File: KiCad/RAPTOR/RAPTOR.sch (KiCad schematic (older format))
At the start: 49 parts, among them J1 SOLC_CONN, J10 EXT_LED3, J11 SRVOL_CONN, J12 SRVOR_CONN, J13 HOTWIRE_CONN, J14 RBF_CONN, J15 EEPROM_BTN_CONN, J16 SOLC_SW_CONN, J17 SOLP_SW_CONN, J18 CONN_BUZZER, J2 SOLP_CONN, J3 JST_2MM_MALE, J4 CONN_LED_FIX, J5 CONN_SOLP_LED, J6 CONN_SOLC_LED, J7 EXT_LED0, J8 EXT_LED1, J9 EXT_LED2, P1 Power, P2 Analog, P3 Digital, P4 Digital, P5 CONN_01X01, P6 CONN_01X01, P7 CONN_01X01, P8 CONN_01X01, Q1 MOSFET-NCH-STQ2NK60ZR-AP, Q2 MOSFET-NCH-STQ2NK60ZR-AP, Q3 MOSFET-NCH-STQ2NK60ZR-AP, Q4 MOSFET-NCH-STQ2NK60ZR-AP, Q5 MOSFET-NCH-STQ2NK60ZR-AP, U1 BMP280 Breakout, U2 BNO055 Breakout, U3 OpenLog, U4 AdafruitGPS, U5 U3V12F12, U6 D24V550F5

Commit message: Added Teensy
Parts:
- removed J16: SOLC_SW_CONN, RAPTOR_footprints:Molex-2pin, symbol RAPTOR-rescue:CONN_02-SparkFun-Connectors
- removed J17: SOLP_SW_CONN, RAPTOR_footprints:Molex-2pin, symbol RAPTOR-rescue:CONN_02-SparkFun-Connectors
- removed J5: CONN_SOLP_LED, RAPTOR_footprints:Molex-2pin, symbol RAPTOR-rescue:CONN_02-SparkFun-Connectors
- removed J6: CONN_SOLC_LED, RAPTOR_footprints:Molex-2pin, symbol RAPTOR-rescue:CONN_02-SparkFun-Connectors
- removed P1: Power, RAPTOR_footprints:Socket_Strip_Arduino_1x08, symbol Connector_Generic:Conn_01x08
- removed P2: Analog, RAPTOR_footprints:Arduino_Analog_06, symbol RAPTOR-rescue:Arduino_Analog_Conn
- removed P3: Digital, RAPTOR_footprints:Arduino_x10_Digital, symbol RAPTOR-rescue:Arduino_Digital_01x10_Conn
- removed P4: Digital, RAPTOR_footprints:Arduino_x08_Digital, symbol RAPTOR-rescue:Arduino_Digital_8
- removed P5, P6, P7, P8: CONN_01X01, Socket_Arduino_Uno:Arduino_1pin, symbol Connector_Generic:Conn_01x01
- removed R3, R4: 100OHM-0603-1_10W-1%, RAPTOR_footprints:Resistor, symbol RAPTOR-rescue:100OHM-0603-1_10W-1%-SparkFun-Resistors
- removed R6, R7: 4.7KOHM-0603-1_10W-1%, RAPTOR_footprints:Resistor, symbol RAPTOR-rescue:4.7KOHM-0603-1_10W-1%-SparkFun-Resistors
- added U?: Teensy3.2, symbol teensy:Teensy3.2
- J15: value EEPROM_BTN_CONN -> EEP_BTN_CONN
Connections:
- net labels added: EEP_BTN
- net labels removed: A4(SDA), A5(SCL), AREF, EEPROM_BTN, IOREF, LEDC_DTA, LEDP_DTA, Reset, SOLC_SW, SOLP_SW
- wire segments 182 -> 139
- no-connect marks 18 -> 13
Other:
- note removed: "1"
- note removed: "Holes"
- note removed: "Shield for Arduino that uses\nthe same pin disposition\nlike "Uno" board Rev 3."
- moved on the sheet: J13, J14, J15, J3, Q5, R5, R8

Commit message: Removed 12v Step Up from schematic.
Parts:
- removed U5: U3V12F12, RAPTOR_footprints:U3V12F12, symbol RAPTOR-rescue:U3V12F12
- U?: symbol teensy:Teensy3.2 -> RAPTOR-rescue:Teensy3.2-teensy
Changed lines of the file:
@@
 EESchema Schematic File Version 4
 LIBS:RAPTOR-cache
-EELAYER 26 0
+EELAYER 30 0
 EELAYER END
 $Descr USLetter 11000 8500
@@
 $EndComp
 $Comp
-L power:GND #PWR012
-U 1 1 5C40FAEF
-P 3550 2400
-F 0 "#PWR012" H 3550 2150 50  0001 C CNN
-F 1 "GND" H 3555 2227 50  0000 C CNN
-F 2 "" H 3550 2400 50  0001 C CNN
-F 3 "" H 3550 2400 50  0001 C CNN
-	1    3550 2400
-	1    0    0    -1
-$EndComp
-Wire Wire Line
-	3550 2250 3550 2400
-$Comp
-L power:+7.5V #PWR011
-U 1 1 5C42772B
-P 3000 1900
-F 0 "#PWR011" H 3000 1750 50  0001 C CNN
-F 1 "+7.5V" H 3015 2073 50  0001 C CNN
-F 2 "" H 3000 1900 50  0001 C CNN
-F 3 "" H 3000 1900 50  0001 C CNN
-F 4 "+7.4V" H 3015 2073 50  0000 C CNN "Real Value"
-	1    3000 1900
-	1    0    0    -1
-$EndComp
-Wire Wire Line
-	3250 1950 3000 1950
-Wire Wire Line
-	3850 1950 4100 1950
-$Comp
-L power:+12V #PWR013
-U 1 1 5C4334FC
-P 4100 1900
-F 0 "#PWR013" H 4100 1750 50  0001 C CNN
-F 1 "+12V" H 4115 2165 50  0000 C CNN
-F 2 "" H 4100 1900 50  0001 C CNN
-F 3 "" H 4100 1900 50  0001 C CNN
-F 4 "(TO SOLENOID)" H 4115 2074 50  0000 C CNN "Note"
-	1    4100 1900
-	1    0    0    -1
-$EndComp
-$Comp
 L power:+5V #PWR014
 U 1 1 5C442A87
@@
 	1    0    0    -1
 $EndComp
-Wire Wire Line
-	3000 1950 3000 1900
-Wire Wire Line
-	4100 1950 4100 1900
 $Comp
 L power:GND #PWR016
@@
 F 3 "" H 4950 3100 50  0001 C CNN
 	1    4950 3100
-	1    0    0    -1
-$EndComp
-$Comp
-L RAPTOR-rescue:U3V12F12 U5
-U 1 1 5C3DF905
-P 3550 1950
-F 0 "U5" H 3550 2192 50  0000 C CNN
-F 1 "U3V12F12" H 3550 2101 50  0000 C CNN
-F 2 "RAPTOR_footprints:U3V12F12" H 3550 2200 50  0001 C CNN
-F 3 "" H 3550 2200 50  0001 C CNN
-	1    3550 1950
 	1    0    0    -1
 $EndComp
@@
 	2800 3500 2650 3500
 $Comp
-L teensy:Teensy3.2 U?
+L RAPTOR-rescue:Teensy3.2-teensy U?
 U 1 1 5D836A4E
 P 9200 2150

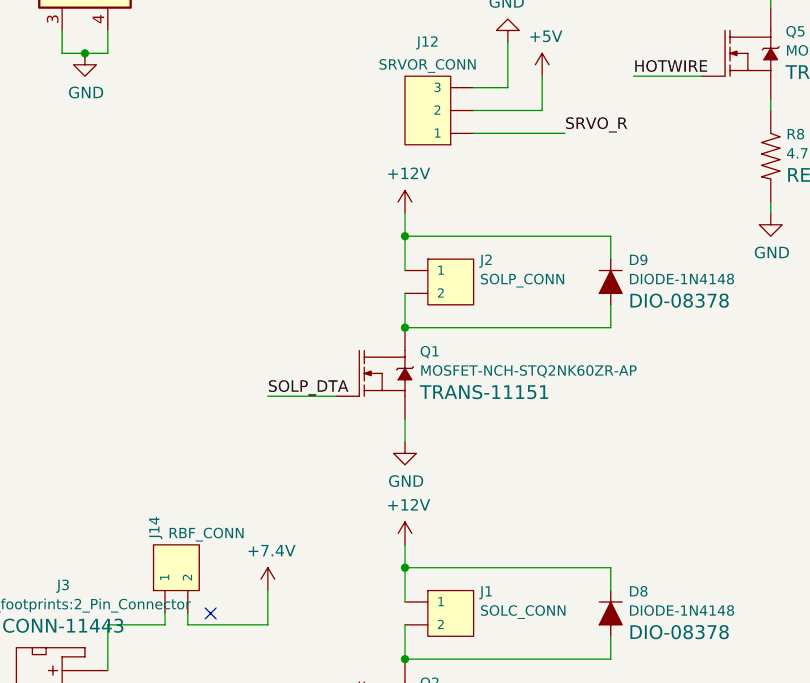
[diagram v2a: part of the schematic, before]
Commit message: Swapped +12V references with +7.4V references.
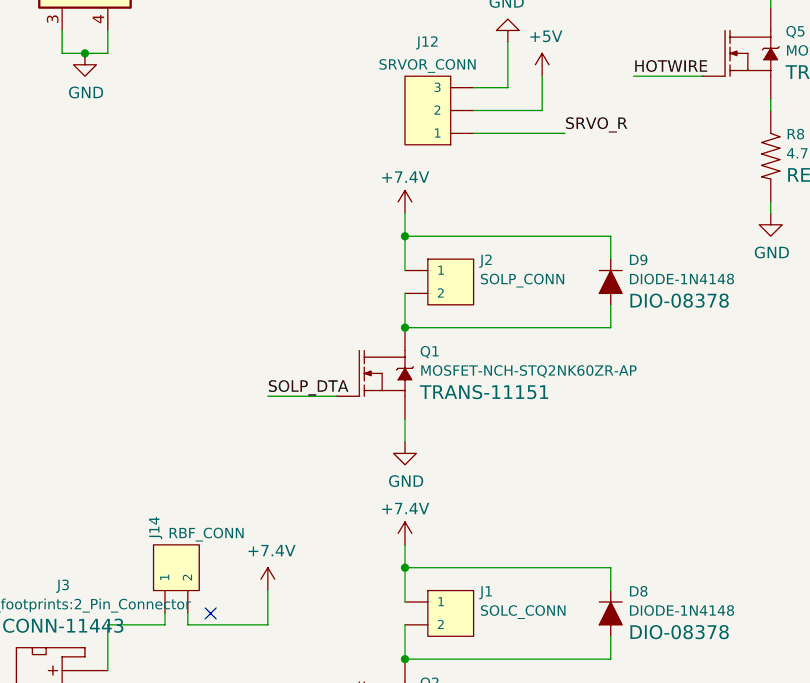
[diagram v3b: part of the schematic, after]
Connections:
- net +12V is gone; now on net +7.5V: D8.C, D9.C, J1.1, J2.1
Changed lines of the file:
@@
 	5550 1000 5550 850
-$Comp
-L power:+12V #PWR0113
-U 1 1 5BE8A086
-P 4950 2100
-F 0 "#PWR0113" H 4950 1950 50  0001 C CNN
-F 1 "+12V" H 4965 2273 50  0000 C CNN
-F 2 "" H 4950 2100 50  0001 C CNN
-F 3 "" H 4950 2100 50  0001 C CNN
-	1    4950 2100
-	1    0    0    -1
-$EndComp
 $Comp
 L RAPTOR-rescue:MOSFET-NCH-2N7002PW-SparkFun-DiscreteSemi Q1
@@
 	5850 2600 4950 2600
 $Comp
-L power:+12V #PWR05
+L power:+7.5V #PWR05
 U 1 1 5C55623C
 P 4950 3550
 F 0 "#PWR05" H 4950 3400 50  0001 C CNN
-F 1 "+12V" H 4965 3723 50  0000 C CNN
+F 1 "+7.5V" H 4965 3723 50  0001 C CNN
 F 2 "" H 4950 3550 50  0001 C CNN
 F 3 "" H 4950 3550 50  0001 C CNN
+F 4 "+7.4V" H 4950 3707 50  0000 C CNN "Real Value"
 	1    4950 3550
 	1    0    0    -1
@@
 Wire Wire Line
 	7950 800  7950 700
+$Comp
+L power:+7.5V #PWR0113
+U 1 1 5BE8A086
+P 4950 2100
+F 0 "#PWR0113" H 4950 1950 50  0001 C CNN
+F 1 "+7.5V" H 4965 2273 50  0001 C CNN
+F 2 "" H 4950 2100 50  0001 C CNN
+F 3 "" H 4950 2100 50  0001 C CNN
+F 4 "+7.4V" H 4950 2257 50  0000 C CNN "Real Value"
+	1    4950 2100
+	1    0    0    -1
+$EndComp
 $EndSCHEMATC

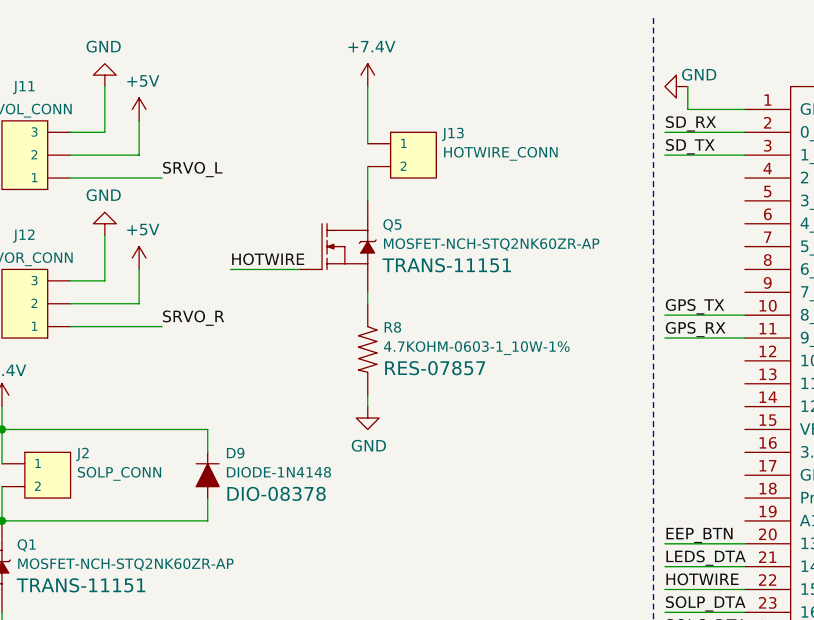
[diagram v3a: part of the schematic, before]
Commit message: Removed unused hotwire subcircuit.
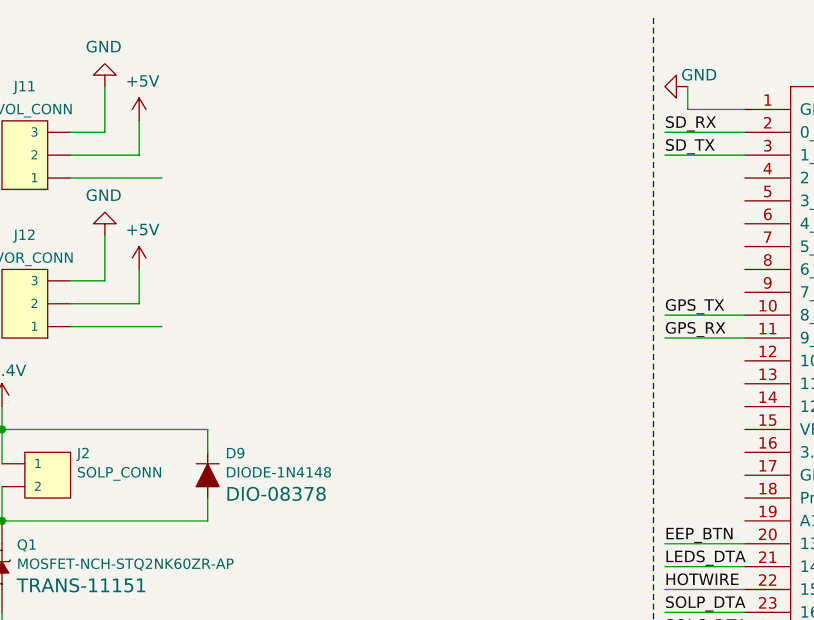
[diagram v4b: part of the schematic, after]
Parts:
- removed J13: HOTWIRE_CONN, RAPTOR_footprints:Molex-2pin, symbol RAPTOR-rescue:CONN_02-SparkFun-Connectors
- removed Q5: MOSFET-NCH-STQ2NK60ZR-AP, RAPTOR_footprints:MOSFET, symbol RAPTOR-rescue:MOSFET-NCH-2N7002PW-SparkFun-DiscreteSemi
- removed R8: 4.7KOHM-0603-1_10W-1%, RAPTOR_footprints:Resistor, symbol RAPTOR-rescue:4.7KOHM-0603-1_10W-1%-SparkFun-Resistors
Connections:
- wire segments 134 -> 129
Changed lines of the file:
@@
 NoConn ~ 1950 800
 NoConn ~ 1950 1300
-Text Label 5650 1750 0    50   ~ 0
-SRVO_R
 Wire Wire Line
 	5250 1750 5650 1750
@@
 Wire Wire Line
 	5550 1650 5550 1500
-Text Label 5650 1100 0    50   ~ 0
-SRVO_L
 Wire Wire Line
 	5250 1100 5650 1100
@@
 $EndComp
 $Comp
-L RAPTOR-rescue:MOSFET-NCH-2N7002PW-SparkFun-DiscreteSemi Q5
-U 1 1 5C45C6C5
-P 6450 1400
-F 0 "Q5" H 6615 1495 45  0000 L CNN
-F 1 "MOSFET-NCH-STQ2NK60ZR-AP" H 6615 1411 45  0000 L CNN
-F 2 "RAPTOR_footprints:MOSFET" H 6450 1700 20  0001 C CNN
-F 3 "https://www.diodes.com/assets/Datasheets/ds11303.pdf" H 6450 1400 50  0001 C CNN
-F 4 "TRANS-11151" H 6615 1316 60  0000 L CNN "Field4"
-	1    6450 1400
-	1    0    0    -1
-$EndComp
-Text Label 5950 1500 0    50   ~ 0
-HOTWIRE
-Wire Wire Line
-	6250 1500 5950 1500
-$Comp
-L power:GND #PWR028
-U 1 1 5C45C6CF
-P 6550 2100
-F 0 "#PWR028" H 6550 1850 50  0001 C CNN
-F 1 "GND" H 6555 1927 50  0000 C CNN
-F 2 "" H 6550 2100 50  0001 C CNN
-F 3 "" H 6550 2100 50  0001 C CNN
-	1    6550 2100
-	1    0    0    -1
-$EndComp
-$Comp
-L RAPTOR-rescue:CONN_02-SparkFun-Connectors J13
-U 1 1 5C45C6DE
-P 6650 950
-F 0 "J13" H 6422 905 45  0000 R CNN
-F 1 "HOTWIRE_CONN" H 6422 989 45  0000 R CNN
-F 2 "RAPTOR_footprints:Molex-2pin" H 6650 1200 20  0001 C CNN
-F 3 "" H 6650 950 50  0001 C CNN
-F 4 "XXX-00000" H 6422 1084 60  0001 R CNN "Field4"
-	1    6650 950
-	-1   0    0    1
-$EndComp
-Wire Wire Line
-	6550 1200 6550 1050
-$Comp
-L RAPTOR-rescue:4.7KOHM-0603-1_10W-1%-SparkFun-Resistors R8
-U 1 1 5C476CBF
-P 6550 1850
-F 0 "R8" V 6455 1918 45  0000 L CNN
-F 1 "4.7KOHM-0603-1_10W-1%" V 6539 1918 45  0000 L CNN
-F 2 "RAPTOR_footprints:Resistor" H 6550 2000 20  0001 C CNN
-F 3 "" H 6550 1850 60  0001 C CNN
-F 4 "RES-07857" V 6634 1918 60  0000 L CNN "Field4"
-	1    6550 1850
-	0    1    1    0
-$EndComp
-Wire Wire Line
-	6550 1600 6550 1650
-Wire Wire Line
-	6550 2050 6550 2100
-Wire Wire Line
-	6550 700  6550 950
-$Comp
-L power:+7.5V #PWR027
-U 1 1 5C4B44D8
-P 6550 700
-F 0 "#PWR027" H 6550 550 50  0001 C CNN
-F 1 "+7.5V" H 6565 873 50  0001 C CNN
-F 2 "" H 6550 700 50  0001 C CNN
-F 3 "" H 6550 700 50  0001 C CNN
-F 4 "+7.4V" H 6565 873 50  0000 C CNN "Real Value"
-	1    6550 700
-	1    0    0    -1
-$EndComp
-$Comp
